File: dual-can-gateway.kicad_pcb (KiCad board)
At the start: 2 copper layers, 101.6 x 88.9 mm, 82 parts, among them J3 Conn_01x02_Pin, Q1 AO3401A, Q2 2N7002, U1 STM32F446RETx, U2 STM32F446RETx, U3 ESP32-WROOM-32UE, U4 TJA1044GT-3, U5 TJA1044GT-3, U6 TJA1055T, U7 TJA1055T, U8 LM2596S-5, U9 AMS1117-3.3

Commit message: hopefully fixed auto wake/shutdown
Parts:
- added R14: 10k, Resistor_SMD:R_0805_2012Metric, F.Cu at (57.6, 72.4)
- added R15: 10k, Resistor_SMD:R_0805_2012Metric, F.Cu at (57.6, 70.2)
- R11: value 100k -> 10k
- moved R8 1.02 mm to (31.0, 73.7)
- renumbered 12V to 12V1, JP-CAN-HS-LISTEN1 to JP-CAN-HS-LISTEN, JP-CAN-HS-MITM1 to JP-CAN-HS-MITM
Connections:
- U1 pad 38: unconnected-(U1-PC7-Pad38) -> Net-(U1-PC7)
- U1 pad 39: unconnected-(U1-PC8-Pad39) -> Net-(U1-PC8)
- U6 pad 5: /3.3V -> Net-(U1-PC7)
- U6 pad 6: /3.3V -> Net-(U1-PC8)
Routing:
- net Net-(U1-PC8): track 0.00 -> 50.2 mm, vias 0 -> 3
- net Net-(U1-PC7): track 0.00 -> 46.2 mm, vias 0 -> 3
- net /GND: track 78.2 -> 92.6 mm, vias 47 -> 49
- net /3.3V: track 422.8 -> 420.1 mm
- net /12V_Raw: track 120.8 -> 122.3 mm
- net Net-(U6-~{ERR}): track 10.5 -> 9.34 mm

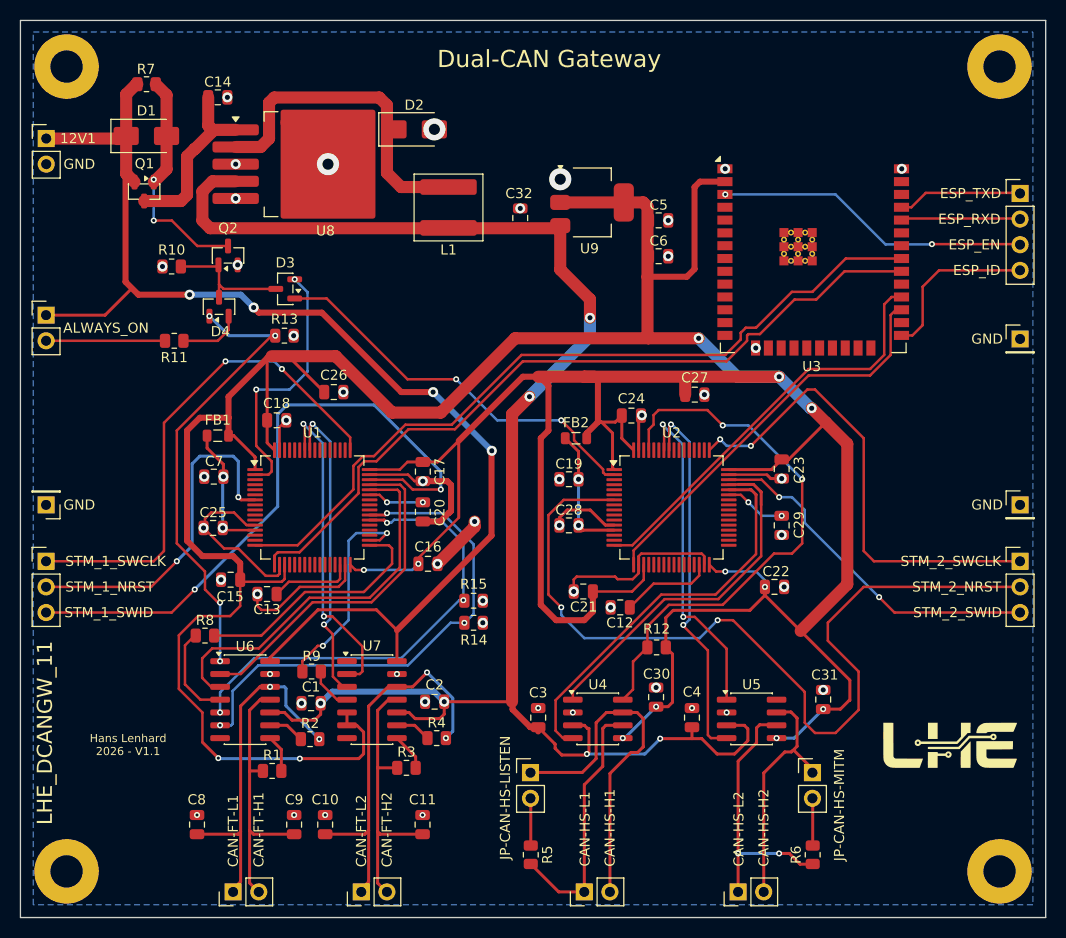
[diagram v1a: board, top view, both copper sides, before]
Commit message: proper caps added
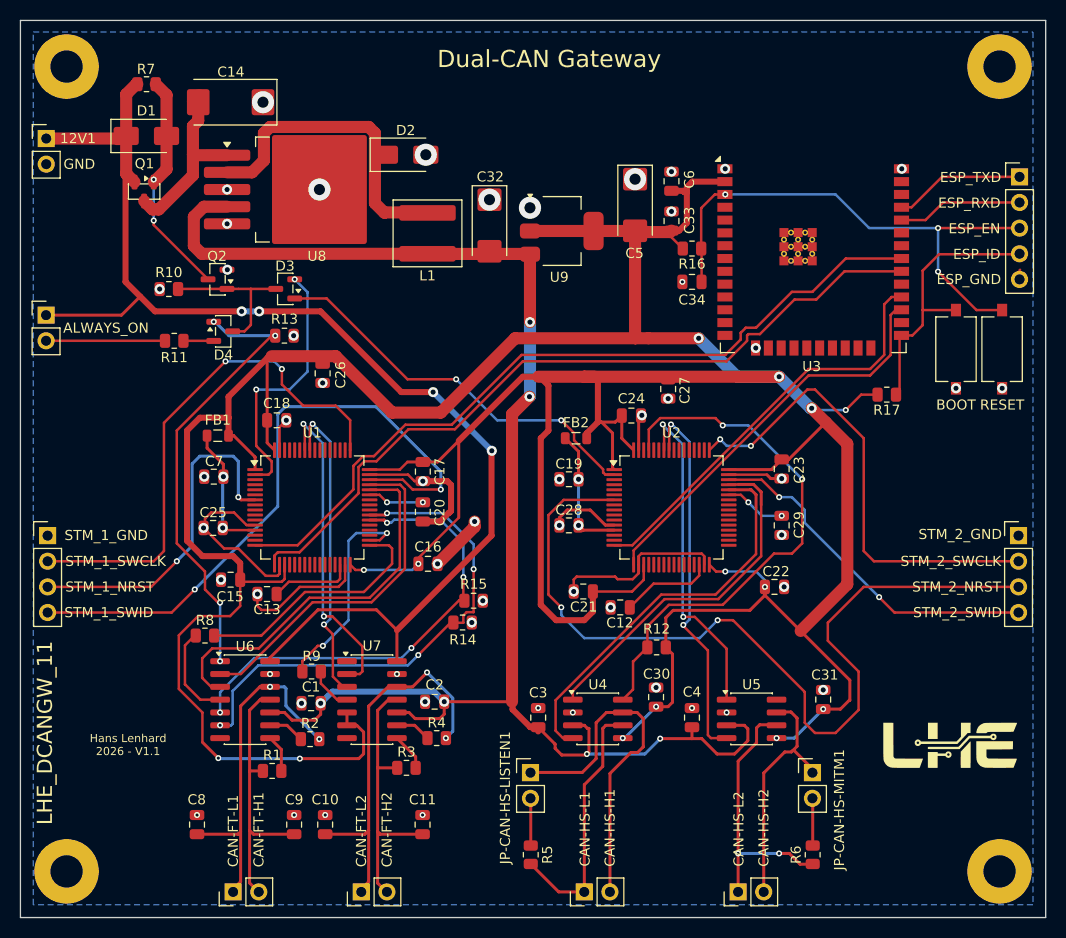
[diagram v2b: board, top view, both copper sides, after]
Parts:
- removed GND (x3): TestPoint, Connector_PinHeader_2.54mm:PinHeader_1x01_P2.54mm_Vertical
- added BOOT: ESP_BOOT, Button_Switch_SMD:SW_Tactile_SPST_NO_Straight_CK_PTS636Sx25SMTRLFS, F.Cu at (105.4, 45.3)
- added C33: 10uF, Capacitor_SMD:C_0805_2012Metric, F.Cu at (77.2, 32.6)
- added C34: 1uF, Capacitor_SMD:C_0805_2012Metric, F.Cu at (79.2, 38.6)
- added R16: 10k, Resistor_SMD:R_0805_2012Metric, F.Cu at (79.2, 35.3)
- added R17: 10k, Resistor_SMD:R_0805_2012Metric, F.Cu at (98.6, 49.8)
- added RESET: ESP_RESET, Button_Switch_SMD:SW_Tactile_SPST_NO_Straight_CK_PTS636Sx25SMTRLFS, F.Cu at (110.0, 45.3)
- C14: value 100pF -> 100uF; footprint Capacitor_SMD:C_0805_2012Metric -> Capacitor_Tantalum_SMD:CP_EIA-7343-40_Kemet-Y_HandSolder
- C32: value 220pF -> 220uF; footprint Capacitor_SMD:C_0805_2012Metric -> Capacitor_Tantalum_SMD:CP_EIA-6032-28_Kemet-C_HandSolder
- C5: value 220 pF -> 220uF; footprint Capacitor_SMD:C_0805_2012Metric -> Capacitor_Tantalum_SMD:CP_EIA-6032-28_Kemet-C_HandSolder
- ESP_FLASH1: value Conn_01x04_Pin -> Conn_01x05_Pin; footprint Connector_PinHeader_2.54mm:PinHeader_1x04_P2.54mm_Vertical -> Connector_PinHeader_2.54mm:PinHeader_1x05_P2.54mm_Vertical
- STM_1_FLASH1, STM_2_FLASH1: value Conn_01x03_Pin -> Conn_01x04_Pin; footprint Connector_PinHeader_2.54mm:PinHeader_1x03_P2.54mm_Vertical -> Connector_PinHeader_2.54mm:PinHeader_1x04_P2.54mm_Vertical
- moved C6 7.54 mm to (77.2, 28.6), turned to 90 degrees
- moved U9 4.12 mm to (66.3, 33.6)
- moved L1 3.30 mm to (53.0, 33.8)
- moved C32 3.14 mm to (59.2, 33.0)
- moved C5 2.79 mm to (73.6, 31.0), turned to -90 degrees
- moved C27 2.70 mm to (76.9, 49.2), turned to -90 degrees
- moved U8 2.65 mm to (40.8, 29.5)
- moved D2 2.65 mm to (50.9, 26.0)
- moved Q2 2.58 mm to (32.2, 38.4), turned to 180 degrees
- moved STM_1_FLASH1 2.54 mm to (15.4, 63.8)
- moved STM_2_FLASH1 2.54 mm to (111.6, 63.8)
- moved D4 2.48 mm to (32.8, 43.5), turned to 0 degrees
- moved R10 2.25 mm to (27.4, 39.3)
- moved C26 2.16 mm to (42.6, 47.7), turned to -90 degrees
- moved ESP_FLASH1 1.65 mm to (111.7, 28.2)
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- renumbered JP-CAN-HS-LISTEN to JP-CAN-HS-LISTEN1, JP-CAN-HS-MITM to JP-CAN-HS-MITM1
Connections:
- net Net-(ESP_FLASH1-Pin_3) renamed /ESP_EN
- net Net-(ESP_FLASH1-Pin_4) renamed /ESP_IO
- R12 pad 2: Net-(U2-PB8) -> /3.3V
- STM_1_FLASH1 pad 1: Net-(STM_1_FLASH1-Pin_1) -> /GND
- STM_2_FLASH1 pad 1: Net-(STM_2_FLASH1-Pin_1) -> /GND
- U1 pad 46: Net-(STM_1_FLASH1-Pin_3) -> Net-(STM_1_FLASH1-Pin_4)
- U1 pad 49: Net-(STM_1_FLASH1-Pin_1) -> Net-(STM_1_FLASH1-Pin_2)
- U1 pad 7: Net-(STM_1_FLASH1-Pin_2) -> Net-(STM_1_FLASH1-Pin_3)
- U2 pad 46: Net-(STM_2_FLASH1-Pin_3) -> Net-(STM_2_FLASH1-Pin_4)
- U2 pad 49: Net-(STM_2_FLASH1-Pin_1) -> Net-(STM_2_FLASH1-Pin_2)
- U2 pad 61: Net-(U2-PB8) -> /3.3V
- U2 pad 7: Net-(STM_2_FLASH1-Pin_2) -> Net-(STM_2_FLASH1-Pin_3)
- U4 pad 8: Net-(U2-PB8) -> /3.3V
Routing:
- net Net-(STM_1_FLASH1-Pin_4): track 0.00 -> 64.8 mm, vias 0 -> 2
- net /3.3V: track 420.1 -> 475.3 mm, vias 13 -> 16
- net Net-(U2-PB8): track 54.9 -> 0.00 mm, vias 2 -> 0
- net Net-(STM_2_FLASH1-Pin_3): track 35.1 -> 86.5 mm
- net Net-(STM_1_FLASH1-Pin_1): track 50.2 -> 0.00 mm, vias 2 -> 0
- net Net-(STM_2_FLASH1-Pin_1): track 47.5 -> 0.00 mm, vias 2 -> 0
- net Net-(STM_2_FLASH1-Pin_2): track 86.5 -> 47.5 mm
- net Net-(STM_2_FLASH1-Pin_4): track 0.00 -> 35.1 mm, vias 0 -> 2
- net Net-(STM_1_FLASH1-Pin_3): track 65.0 -> 34.7 mm
- net /ESP_EN: track 31.3 -> 53.1 mm, vias 2 -> 3
- net Net-(STM_1_FLASH1-Pin_2): track 34.7 -> 52.1 mm
- net /ESP_IO: track 16.7 -> 27.6 mm
- net /5V: track 161.8 -> 155.4 mm
- net Net-(D4-Pad2): track 6.29 -> 3.41 mm
- net Net-(Q2-G): track 12.8 -> 15.7 mm
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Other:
- board text added: "ESP_GND"
- board text added: "STM_1_GND"
- board text added: "STM_2_GND"
- board text removed: "C14"

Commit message: we're getting there
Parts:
- removed STM_1_FLASH1, STM_2_FLASH1: Conn_01x04_Pin, Connector_PinHeader_2.54mm:PinHeader_1x04_P2.54mm_Vertical
- added C35: 100nf, Capacitor_SMD:C_0805_2012Metric, F.Cu at (96.3, 67.7)
- added C36: 100nf, Capacitor_SMD:C_0805_2012Metric, F.Cu at (27.9, 68.0)
- added R18: 10k, Resistor_SMD:R_0805_2012Metric, F.Cu at (44.0, 52.2)
- added STM_FLASH1: Conn_01x05_Pin, Connector_PinHeader_2.54mm:PinHeader_1x05_P2.54mm_Vertical, F.Cu at (15.4, 61.2)
- added STM_FLASH2: Conn_01x05_Pin, Connector_PinHeader_2.54mm:PinHeader_1x05_P2.54mm_Vertical, F.Cu at (111.6, 61.1)
- L1: value 33-68 pH -> 33-68 uH
- U1, U2: value STM32F446RETx -> STM32F405RGTx
- U6, U7: value TJA1055T -> TJA1055T/3
- moved R12 24.5 mm to (81.9, 51.1)
- moved C13 9.59 mm to (46.7, 70.4), turned to 180 degrees
- moved C12 9.28 mm to (81.4, 70.4), turned to 180 degrees
- moved C29 3.61 mm to (88.6, 59.2), turned to 90 degrees
- moved C22 2.46 mm to (88.4, 66.6)
- moved C20 2.41 mm to (53.5, 59.2), turned to 90 degrees
- moved C17 2.21 mm to (53.5, 55.4), turned to 90 degrees
- moved C23 1.85 mm to (88.7, 55.4), turned to 90 degrees
- moved C21 1.31 mm to (69.2, 68.2)
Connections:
- C20 pad 1: Net-(U1-PA10) -> /GND
- C20 pad 2: /GND -> Net-(U1-VCAP_2)
- C29 pad 1: Net-(U2-PA10) -> /GND
- C29 pad 2: /GND -> Net-(U2-VCAP_2)
- H1 pad 1: unconnected-(H1-Pad1) -> /GND
- H3 pad 1: unconnected-(H3-Pad1) -> /GND
- H4 pad 1: unconnected-(H4-Pad1) -> /GND
- R12 pad 1: /3.3V -> /GND
- R12 pad 2: /3.3V -> Net-(U2-BOOT0)
- R8 pad 1: Net-(U1-PB12) -> Net-(U1-PB11)
- R9 pad 1: Net-(U1-PB13) -> Net-(U1-PB12)
- U1 pad 30: Net-(U1-VCAP_1) -> Net-(U1-PB11)
- U1 pad 31: /GND -> Net-(U1-VCAP_1)
- U1 pad 34: Net-(U1-PB13) -> unconnected-(U1-PB13-Pad34)
- U1 pad 43: Net-(U1-PA10) -> unconnected-(U1-PA10-Pad43)
- U1 pad 47: /GND -> Net-(U1-VCAP_2)
- U1 pad 60: unconnected-(U1-BOOT0-Pad60) -> Net-(U1-BOOT0)
- U2 pad 30: Net-(U2-VCAP_1) -> unconnected-(U2-PB11-Pad30)
- U2 pad 31: /GND -> Net-(U2-VCAP_1)
- U2 pad 43: Net-(U2-PA10) -> unconnected-(U2-PA10-Pad43)
- U2 pad 47: /GND -> Net-(U2-VCAP_2)
- U2 pad 60: unconnected-(U2-BOOT0-Pad60) -> Net-(U2-BOOT0)
- U2 pad 61: /3.3V -> unconnected-(U2-PB8-Pad61)
- U4 pad 8: /3.3V -> /GND
- U5 pad 8: unconnected-(U5-S-Pad8) -> /GND
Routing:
- net /GND: track 90.7 -> 20.7 mm, vias 53 -> 63
- net Net-(STM_FLASH2-Pin_4): track 86.5 -> 63.8 mm, vias 2 -> 4
- net Net-(U1-PB13): track 21.3 -> 0.00 mm, vias 2 -> 0
- net Net-(U1-PB11): track 0.00 -> 17.5 mm
- net /3.3V: track 475.3 -> 460.5 mm
- net Net-(U2-BOOT0): track 0.00 -> 9.17 mm
- net Net-(U1-VCAP_2): track 0.00 -> 6.39 mm
- net Net-(U1-BOOT0): track 0.00 -> 6.26 mm
- net Net-(U2-PA10): track 6.11 -> 0.00 mm, vias 2 -> 0
- net Net-(U2-VCAP_2): track 0.00 -> 5.94 mm
- net Net-(U2-VCAP_1): track 9.26 -> 3.36 mm
- net Net-(STM_FLASH1-Pin_5): track 64.8 -> 59.1 mm
- net Net-(U1-PA10): track 5.58 -> 0.00 mm, vias 2 -> 0
- net Net-(U1-VCAP_1): track 8.32 -> 4.17 mm
- net Net-(U2-PA12): track 35.0 -> 38.4 mm
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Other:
- board text added: "STM_1_3.3V"
- board text added: "STM_2_3.3V"

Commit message: v1.1 almost done, new preview
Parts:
- added C37: 100nF, Capacitor_SMD:C_0805_2012Metric, F.Cu at (41.3, 29.7)
- added D5: SMCJ24CA, Diode_SMD:D_SMC, F.Cu at (27.2, 21.0)
- added G***: LOGO_DUAL_CAN, mylib:logo_dual_can_12mm, F.Cu at (71.1, 20.3)
- added R19: 10k, Resistor_SMD:R_0805_2012Metric, F.Cu at (37.5, 31.8)
- C14: footprint Capacitor_Tantalum_SMD:CP_EIA-7343-40_Kemet-Y_HandSolder -> Capacitor_SMD:CP_Elec_6.3x7.7
- moved R7 15.8 mm to (24.1, 34.8)
- moved U8 11.8 mm to (49.1, 21.0), turned to 90 degrees
- moved D1 11.3 mm to (32.1, 33.1), turned to 180 degrees
- moved D2 11.0 mm to (57.3, 35.0), turned to 90 degrees
- moved C32 9.44 mm to (57.8, 23.7)
- moved Q1 5.37 mm to (30.1, 28.2), turned to 0 degrees
- moved L1 4.97 mm to (49.1, 36.8), turned to 0 degrees
- moved C14 3.71 mm to (37.2, 20.0), turned to -90 degrees
- moved U9 0.30 mm to (66.3, 33.9)
- renumbered JP-CAN-HS-LISTEN1 to JP-CAN-HS1, JP-CAN-HS-MITM1 to JP-CAN-HS2
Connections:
- net /12V_Raw renamed /12V_Protected
- Q1 pad 1: Net-(D1-A) -> Net-(Q1-G)
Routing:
- net Net-(Q1-G): track 0.00 -> 11.9 mm, vias 0 -> 4
- net /12V_Protected: track 120.7 -> 130.1 mm
- net /12V_Switched: track 18.3 -> 22.4 mm
- net /GND: track 20.7 -> 17.0 mm, vias 63 -> 84
- net Net-(D2-K): track 32.1 -> 28.6 mm
- net /5V: track 155.4 -> 152.2 mm
- net /3.3V: track 460.5 -> 458.8 mm
- net Net-(D1-A): track 22.8 -> 23.8 mm, vias 2 -> 0
- added copper zone on F.Cu, net /3.3V
- added copper zone on F.Cu, net /GND
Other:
- board text removed: "Dual-CAN Gateway"

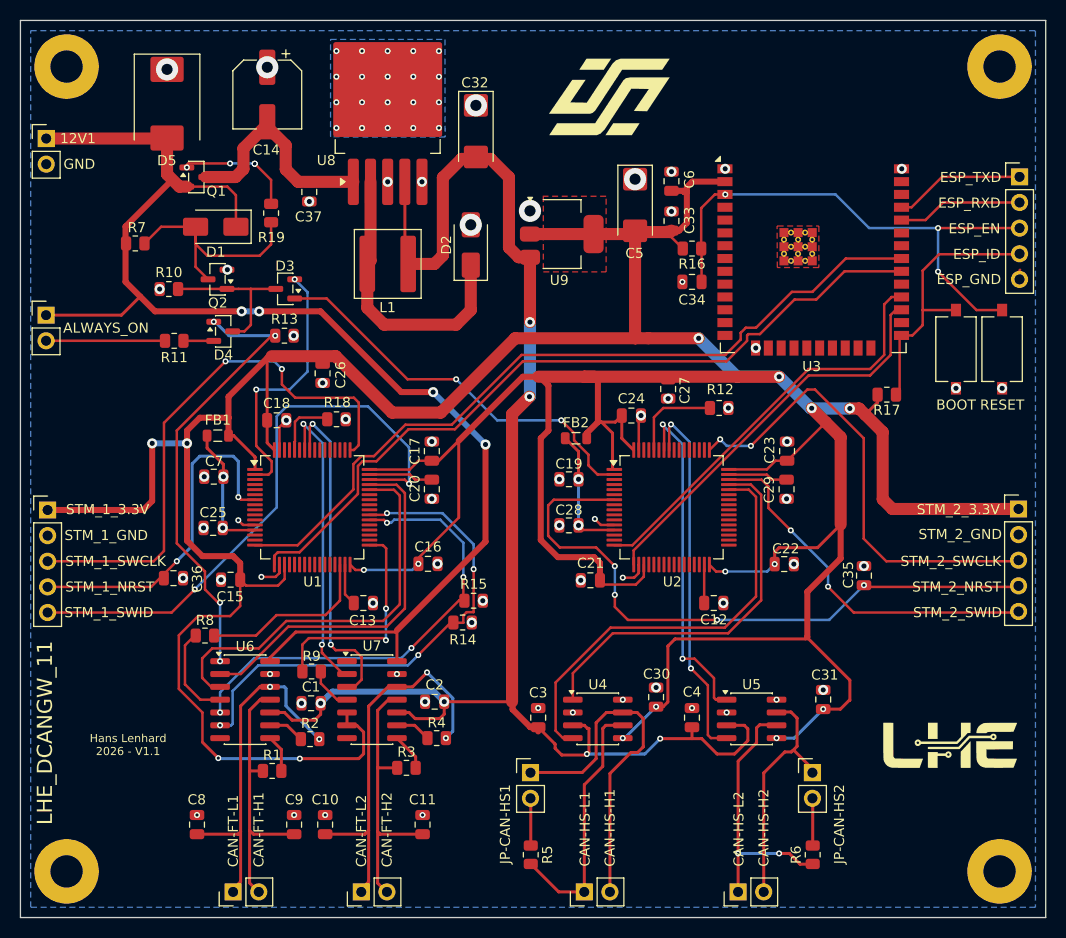
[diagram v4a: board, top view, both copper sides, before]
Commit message: added inter mcu communication as well as debug led
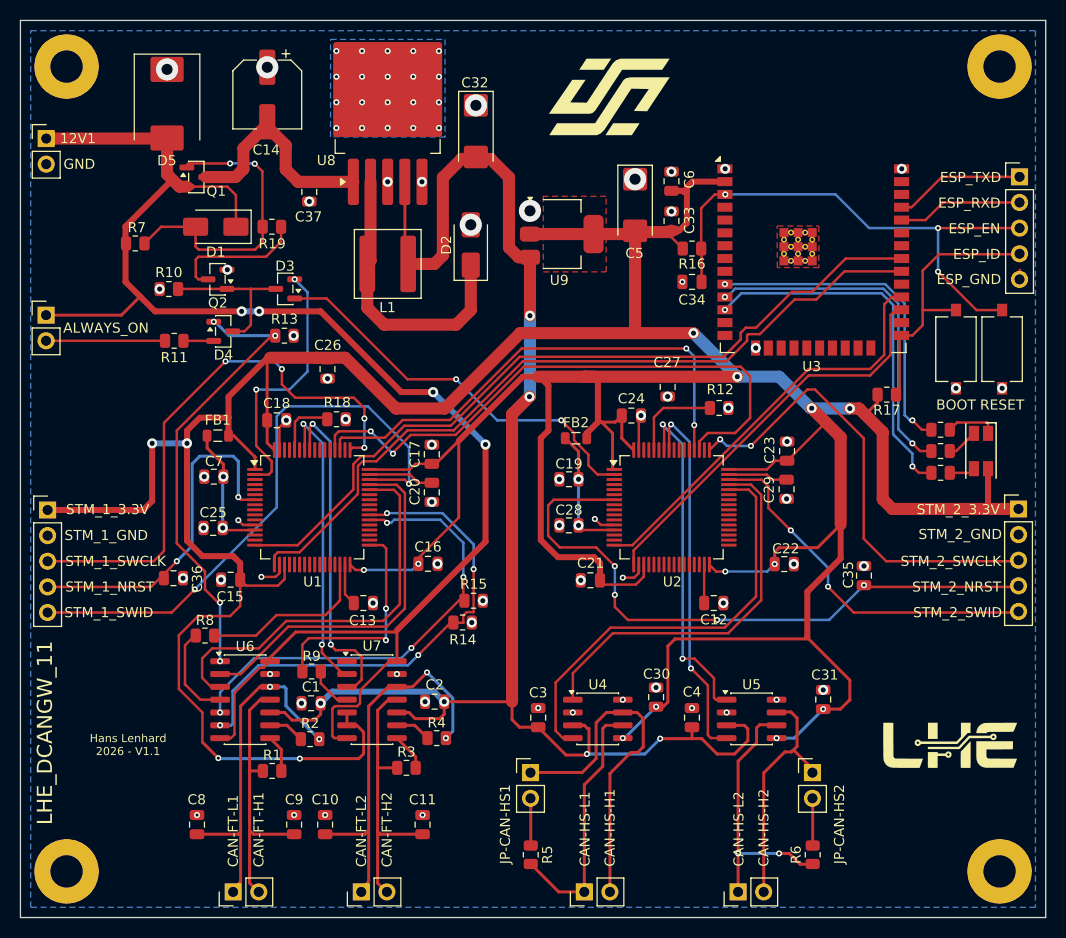
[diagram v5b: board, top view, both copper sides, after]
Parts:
- added D6: LED_RGBA, LED_SMD:LED_RGB_1210, F.Cu at (107.9, 55.4)
- added R20: 1k, Resistor_SMD:R_0805_2012Metric, F.Cu at (103.9, 53.3)
- added R21: 1k, Resistor_SMD:R_0805_2012Metric, F.Cu at (103.9, 55.4)
- added R22: 1k, Resistor_SMD:R_0805_2012Metric, F.Cu at (103.9, 57.5)
- moved R19 1.36 mm to (37.6, 33.1), turned to 180 degrees
- moved C26 0.65 mm to (43.1, 47.2)
- moved C17 0.31 mm to (53.5, 55.7)
- moved C20 0.31 mm to (53.5, 59.5)
- moved C27 0.21 mm to (76.8, 49.0)
- renumbered CAN-FT-LISTEN1 to CAN-FT1, CAN-FT-MITM1 to CAN-FT2, CAN-HS-LISTEN1 to CAN-HS1, CAN-HS-MITM1 to CAN-HS2
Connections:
- Q1 pad 1: Net-(Q1-G) -> Net-(D1-A)
- Q2 pad 3: Net-(D1-A) -> Net-(Q2-D)
- R19 pad 1: Net-(D1-A) -> Net-(Q2-D)
- R19 pad 2: Net-(Q1-G) -> Net-(D1-A)
- U1 pad 51: unconnected-(U1-PC10-Pad51) -> Net-(U1-PC10)
- U1 pad 52: unconnected-(U1-PC11-Pad52) -> Net-(U1-PC11)
- U2 pad 51: unconnected-(U2-PC10-Pad51) -> Net-(U1-PC11)
- U2 pad 52: unconnected-(U2-PC11-Pad52) -> Net-(U1-PC10)
- U3 pad 10: unconnected-(U3-IO25-Pad10) -> Net-(U3-IO25)
- U3 pad 11: unconnected-(U3-IO26-Pad11) -> Net-(U3-IO26)
- U3 pad 12: unconnected-(U3-IO27-Pad12) -> Net-(U3-IO27)
- U6 pad 7: unconnected-(U6-~{WAKE}-Pad7) -> /12V_Protected
- U7 pad 7: unconnected-(U7-~{WAKE}-Pad7) -> /12V_Protected
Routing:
- net Net-(U1-PC11): track 0.00 -> 58.7 mm, vias 0 -> 2
- net Net-(U1-PC10): track 0.00 -> 49.6 mm, vias 0 -> 2
- net Net-(U3-IO27): track 0.00 -> 36.8 mm, vias 0 -> 2
- net Net-(U3-IO26): track 0.00 -> 34.5 mm, vias 0 -> 2
- net Net-(U3-IO25): track 0.00 -> 32.9 mm, vias 0 -> 2
- net /12V_Protected: track 130.1 -> 153.9 mm
- net Net-(Q2-D): track 0.00 -> 13.7 mm
- net Net-(Q1-G): track 11.9 -> 0.00 mm, vias 4 -> 0
- net Net-(D1-A): track 23.8 -> 30.1 mm, vias 0 -> 2
- net Net-(D6-RK): track 0.00 -> 5.12 mm
- net Net-(D6-GK): track 0.00 -> 3.11 mm
- net Net-(D6-BK): track 0.00 -> 2.56 mm
- net Net-(STM_FLASH1-Pin_3): track 54.5 -> 55.4 mm, vias 2 -> 4

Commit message: print ready?
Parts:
- moved C31 4.59 mm to (88.6, 77.2)
- moved C3 3.42 mm to (66.3, 79.2)
- moved C30 2.62 mm to (75.4, 77.2)
- moved R5 2.29 mm to (65.6, 95.4)
- moved CAN-HS1 2.29 mm to (70.9, 99.1)
- moved JP-CAN-HS1 2.29 mm to (65.5, 87.2)
- moved U4 2.29 mm to (72.2, 81.9)
- moved C6 1.37 mm to (78.5, 28.1)
- moved C34 1.15 mm to (79.1, 39.8)
- moved R16 1.15 mm to (79.1, 36.4)
- moved C36 1.02 mm to (28.6, 67.3)
- moved C4 0.51 mm to (78.7, 81.8)
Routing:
- net /3.3V: track 458.7 -> 454.1 mm
- net /5V: track 152.2 -> 153.9 mm
- net Net-(U1-PA2): track 77.7 -> 76.2 mm
- net Net-(U1-PA3): track 76.7 -> 75.4 mm
- net /ESP_EN: track 53.1 -> 54.3 mm
- net Net-(U2-PA11): track 43.0 -> 42.1 mm
- net Net-(U2-PA12): track 38.4 -> 37.5 mm
